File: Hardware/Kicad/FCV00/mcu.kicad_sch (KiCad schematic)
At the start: 35 parts, among them J1 USB_C_GCT_USB4105-GF-A, SW1 BOOT, U5 STM32F405RGT6, Y1 8MHz 12pF

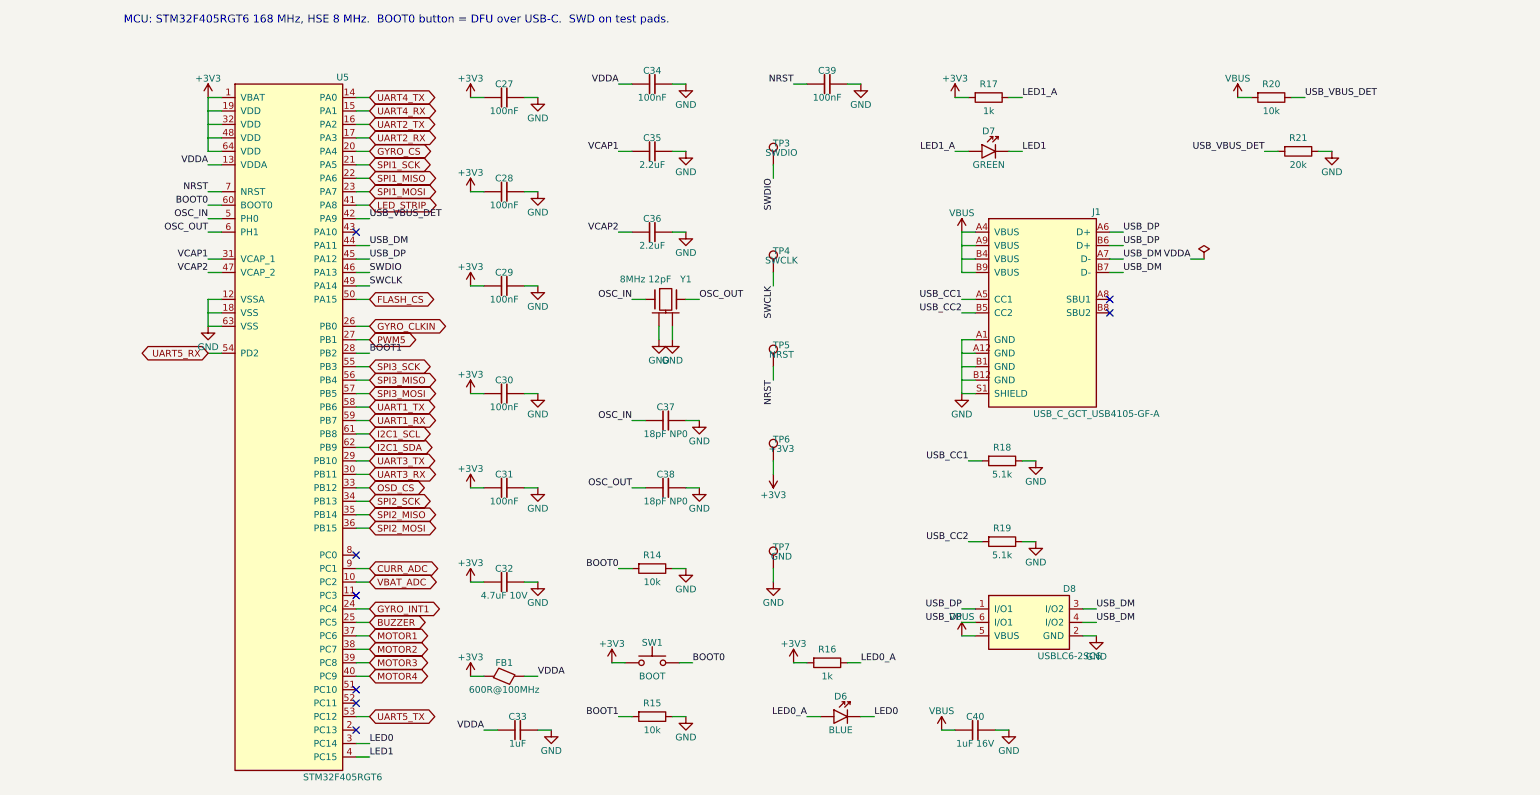
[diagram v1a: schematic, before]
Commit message: Boards follow the B0_EE part convention
- every real part uses the symbol/footprint/3D/datasheet named after its MPN in Kicad_Libs
- symbols keep only Reference, Value, Footprint, Datasheet, Description
  (MPN, Manufacturer, Verify, LCSC, Note fields removed; Verify notes moved to the Readme)
- schematic symbol caches rebuilt from the libraries, PCB footprints relinked with the
  same fields and 3D models as the library (connectivity unchanged)
- DNP and BOM attributes of the footprints match the symbols
- BOMs re-exported with kicad-cli
- ignore KiCad local history
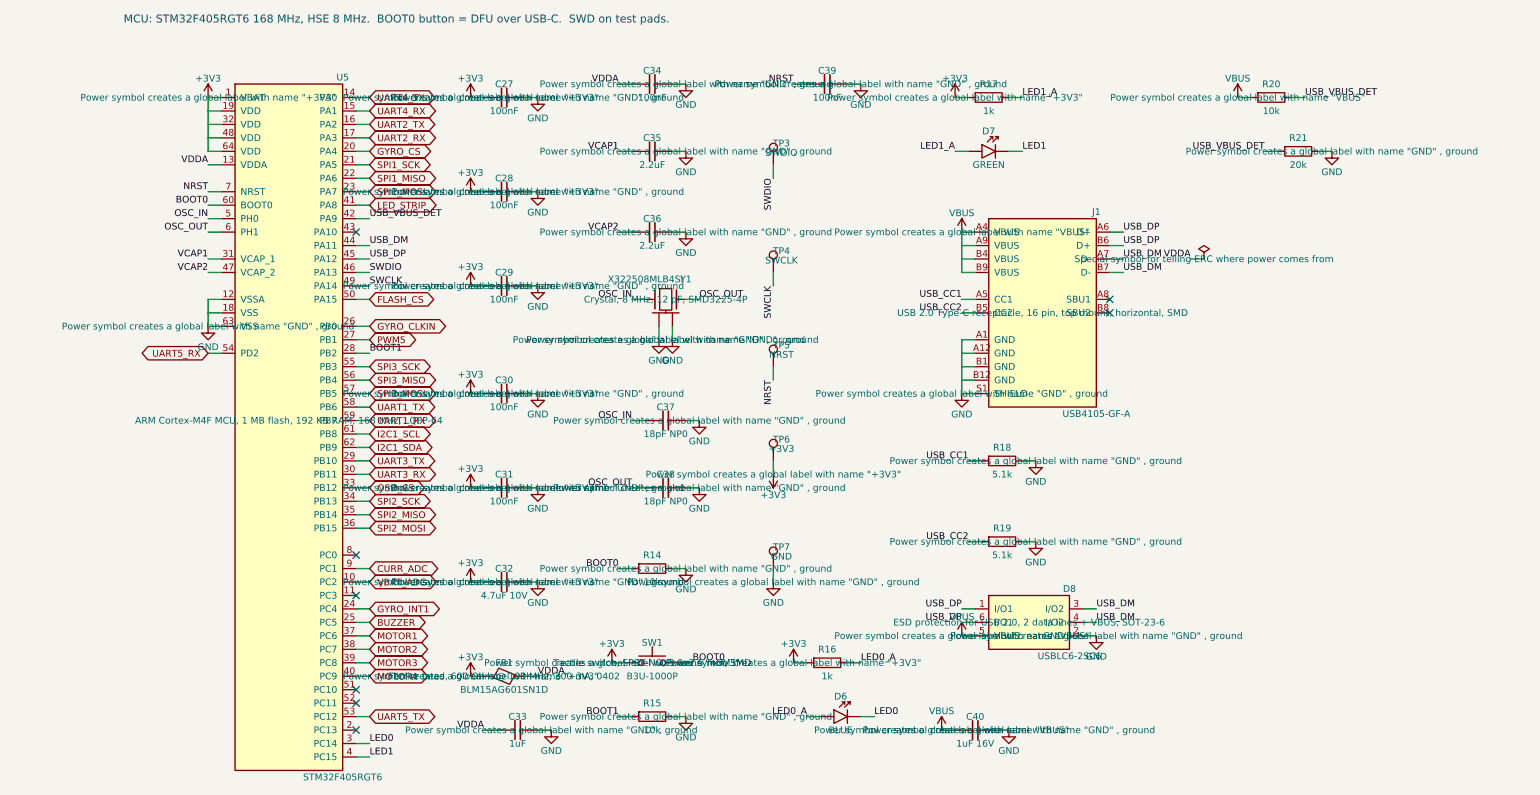
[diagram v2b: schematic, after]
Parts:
- D8: footprint eDiodes:SOT-23-6 -> eDiodes:USBLC6-2SC6; LCSC C7519 -> (none); MPN USBLC6-2SC6 -> (none); Manufacturer STMicroelectronics -> (none)
- FB1: value 600R@100MHz -> BLM15AG601SN1D; footprint eChoke:L_0402_1005Metric -> eFerrite:BLM15AG601SN1D; symbol eChoke:FB -> eFerrite:BLM15AG601SN1D; MPN BLM15AG601SN1D -> (none)
- J1: value USB_C_GCT_USB4105-GF-A -> USB4105-GF-A; footprint eConnector:USB_C_Receptacle_GCT_USB4105-xx-A_16P_TopMnt_Horizontal -> eConnector:USB4105-GF-A; symbol eConnector:USB_C_GCT_USB4105-GF-A -> eConnector:USB4105-GF-A; MPN USB4105-GF-A -> (none); Manufacturer GCT -> (none)
- SW1: value BOOT -> B3U-1000P; footprint eSwitch:SW_SPST_B3U-1000P -> eSwitch:B3U-1000P; symbol eSwitch:SW_Push -> eSwitch:B3U-1000P; MPN B3U-1000P -> (none); Manufacturer Omron -> (none)
- TP3, TP4, TP5, TP6, TP7: now left out of the parts list
- U5: footprint eMCU:LQFP-64_10x10mm_P0.5mm -> eMCU:STM32F405RGT6; LCSC C15742 -> (none); MPN STM32F405RGT6 -> (none); Manufacturer STMicroelectronics -> (none)
- Y1: value 8MHz 12pF -> X322508MLB4SI; footprint eCrystal:Crystal_SMD_3225-4Pin_3.2x2.5mm -> eCrystal:X322508MLB4SI; symbol eCrystal:Crystal_GND24 -> eCrystal:X322508MLB4SI; MPN X322508MLB4SI -> (none); Manufacturer Yangxing -> (none)

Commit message: Cleared all the descriptions and started Power section for FCV
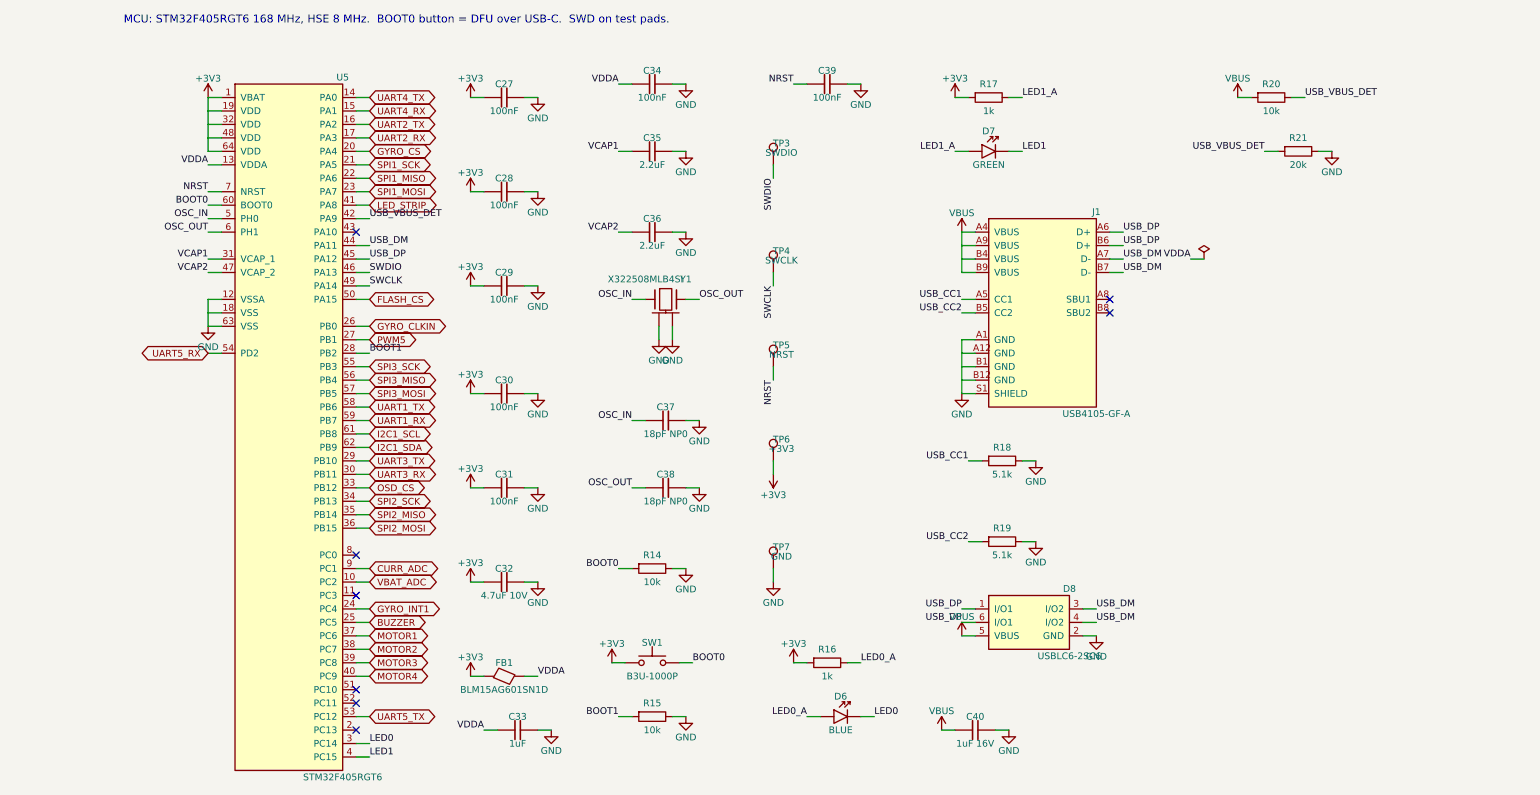
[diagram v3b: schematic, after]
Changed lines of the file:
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@@
 		(property "Description" "Power symbol creates a global label with name \"+3V3\""
 			(at 77.47 139.7 0)
+			(hide yes)
 			(show_name no)
 			(do_not_autoplace no)
@@
 		(property "Description" "Power symbol creates a global label with name \"GND\" , ground"
 			(at 120.65 91.44 0)
+			(hide yes)
 			(show_name no)
 			(do_not_autoplace no)
@@
 		(property "Description" "Crystal, 8 MHz, 12 pF, SMD3225-4P"
 			(at 114.3 68.58 0)
+			(hide yes)
 			(show_name no)
 			(do_not_autoplace no)
@@
 		(property "Description" "Power symbol creates a global label with name \"GND\" , ground"
 			(at 118.11 40.64 0)
+			(hide yes)
 			(show_name no)
 			(do_not_autoplace no)
@@
 		(property "Description" "Power symbol creates a global label with name \"+3V3\""
 			(at 77.47 86.36 0)
+			(hide yes)
 			(show_name no)
 			(do_not_autoplace no)
@@
 		(property "Description" "Power symbol creates a global label with name \"VBUS\""
 			(at 222.25 30.48 0)
+			(hide yes)
 			(show_name no)
 			(do_not_autoplace no)
@@
 		(property "Description" "Power symbol creates a global label with name \"GND\" , ground"
 			(at 90.17 48.26 0)
+			(hide yes)
 			(show_name no)
 			(do_not_autoplace no)
@@
 		(property "Description" "Power symbol creates a global label with name \"GND\" , ground"
 			(at 115.57 76.2 0)
+			(hide yes)
 			(show_name no)
 			(do_not_autoplace no)
@@
 		(property "Description" "Power symbol creates a global label with name \"GND\" , ground"
 			(at 92.71 149.86 0)
+			(hide yes)
 			(show_name no)
 			(do_not_autoplace no)
@@
 		(property "Description" "Power symbol creates a global label with name \"GND\" , ground"
 			(at 179.07 149.86 0)
+			(hide yes)
 			(show_name no)
 			(do_not_autoplace no)
@@
 		(property "Description" "Power symbol creates a global label with name \"GND\" , ground"
 			(at 90.17 121.92 0)
+			(hide yes)
 			(show_name no)
 			(do_not_autoplace no)
@@
 		(property "Description" "Special symbol for telling ERC where power comes from"
 			(at 215.9 60.96 0)
+			(hide yes)
 			(show_name no)
 			(do_not_autoplace no)
@@
 		(property "Description" "Power symbol creates a global label with name \"GND\" , ground"
 			(at 134.62 121.92 0)
+			(hide yes)
 			(show_name no)
 			(do_not_autoplace no)
@@
 		(property "Description" "Power symbol creates a global label with name \"+3V3\""
 			(at 134.62 101.6 0)
+			(hide yes)
 			(show_name no)
 			(do_not_autoplace no)
@@
 		(property "Description" "Power symbol creates a global label with name \"GND\" , ground"
 			(at 90.17 104.14 0)
+			(hide yes)
 			(show_name no)
 			(do_not_autoplace no)
@@
 		(property "Description" "Power symbol creates a global label with name \"GND\" , ground"
 			(at 151.13 27.94 0)
+			(hide yes)
 			(show_name no)
 			(do_not_autoplace no)
@@
 		(property "Description" "Power symbol creates a global label with name \"GND\" , ground"
 			(at 113.03 76.2 0)
+			(hide yes)
 			(show_name no)
 			(do_not_autoplace no)
@@
 		(property "Description" "Power symbol creates a global label with name \"GND\" , ground"
 			(at 118.11 119.38 0)
+			(hide yes)
 			(show_name no)
 			(do_not_autoplace no)
@@
 		(property "Description" "Power symbol creates a global label with name \"+3V3\""
 			(at 104.14 137.16 0)
+			(hide yes)
 			(show_name no)
 			(do_not_autoplace no)
@@
 		(property "Description" "Power symbol creates a global label with name \"GND\" , ground"
 			(at 170.18 86.36 0)
+			(hide yes)
 			(show_name no)
 			(do_not_autoplace no)
@@
 		(property "Description" "Power symbol creates a global label with name \"GND\" , ground"
 			(at 90.17 86.36 0)
+			(hide yes)
 			(show_name no)
 			(do_not_autoplace no)
@@
 		(property "Description" "Ferrite bead, 600 Ohm @ 100 MHz, 300 mA, 0402"
 			(at 83.82 139.7 0)
+			(hide yes)
 			(show_name no)
 			(do_not_autoplace no)
@@
 		(property "Description" "Power symbol creates a global label with name \"+3V3\""
 			(at 77.47 121.92 0)
+			(hide yes)
 			(show_name no)
 			(do_not_autoplace no)
@@
 		(property "Description" "USB 2.0 Type-C receptacle, 16 pin, top mount, horizontal, SMD"
 			(at 185.42 71.12 0)
+			(hide yes)
 			(show_name no)
 			(do_not_autoplace no)
@@
 		(property "Description" "Power symbol creates a global label with name \"+3V3\""
 			(at 138.43 137.16 0)
+			(hide yes)
 			(show_name no)
 			(do_not_autoplace no)
@@
 		(property "Description" "Power symbol creates a global label with name \"GND\" , ground"
 			(at 240.03 40.64 0)
+			(hide yes)
 			(show_name no)
 			(do_not_autoplace no)
@@
 		(property "Description" "Power symbol creates a global label with name \"VBUS\""
 			(at 166.37 149.86 0)
+			(hide yes)
 			(show_name no)
 			(do_not_autoplace no)
@@
 		(property "Description" "Power symbol creates a global label with name \"GND\" , ground"
 			(at 118.11 147.32 0)
+			(hide yes)
 			(show_name no)
 			(do_not_autoplace no)
@@
 		(property "Description" "Power symbol creates a global label with name \"GND\" , ground"
 			(at 184.15 114.3 0)
+			(hide yes)
 			(show_name no)
 			(do_not_autoplace no)
@@
 		(property "Description" "Power symbol creates a global label with name \"VBUS\""
 			(at 170.18 55.88 0)
+			(hide yes)
 			(show_name no)
 			(do_not_autoplace no)
@@
 		(property "Description" "Power symbol creates a global label with name \"+3V3\""
 			(at 168.91 30.48 0)
+			(hide yes)
 			(show_name no)
 			(do_not_autoplace no)
@@
 		(property "Description" "Power symbol creates a global label with name \"+3V3\""
 			(at 27.94 30.48 0)
+			(hide yes)
 			(show_name no)
 			(do_not_autoplace no)
@@
 		(property "Description" "Power symbol creates a global label with name \"+3V3\""
 			(at 77.47 30.48 0)
+			(hide yes)
 			(show_name no)
 			(do_not_autoplace no)
@@
 		(property "Description" "Power symbol creates a global label with name \"VBUS\""
 			(at 170.18 132.08 0)
+			(hide yes)
 			(show_name no)
 			(do_not_autoplace no)
@@
 		(property "Description" "ESD protection for USB 2.0, 2 data lines + VBUS, SOT-23-6"
 			(at 182.88 129.54 0)
+			(hide yes)
 			(show_name no)
 			(do_not_autoplace no)
@@
 		(property "Description" "Power symbol creates a global label with name \"+3V3\""
 			(at 77.47 66.04 0)
+			(hide yes)
 			(show_name no)
 			(do_not_autoplace no)
@@
 		(property "Description" "Power symbol creates a global label with name \"GND\" , ground"
 			(at 120.65 104.14 0)
+			(hide yes)
 			(show_name no)
 			(do_not_autoplace no)
@@
 		(property "Description" "Power symbol creates a global label with name \"GND\" , ground"
 			(at 27.94 73.66 0)
+			(hide yes)
 			(show_name no)
 			(do_not_autoplace no)
@@
 		(property "Description" "Power symbol creates a global label with name \"GND\" , ground"
 			(at 118.11 55.88 0)
+			(hide yes)
 			(show_name no)
 			(do_not_autoplace no)
@@
 		(property "Description" "Power symbol creates a global label with name \"GND\" , ground"
 			(at 90.17 30.48 0)
+			(hide yes)
 			(show_name no)
 			(do_not_autoplace no)
@@
 		(property "Description" "Power symbol creates a global label with name \"GND\" , ground"
 			(at 118.11 27.94 0)
+			(hide yes)
 			(show_name no)
 			(do_not_autoplace no)
@@
 		(property "Description" "Power symbol creates a global label with name \"GND\" , ground"
 			(at 195.58 132.08 0)
+			(hide yes)
 			(show_name no)
 			(do_not_autoplace no)
@@
 		(property "Description" "ARM Cortex-M4F MCU, 1 MB flash, 192 KB RAM, 168 MHz, LQFP-64"
 			(at 43.18 91.44 0)
+			(hide yes)
 			(show_name no)
 			(do_not_autoplace no)
@@
 		(property "Description" "Tactile switch, SPST-NO, 3.0x2.5 mm, SMD"
 			(at 111.76 137.16 0)
+			(hide yes)
 			(show_name no)
 			(do_not_autoplace no)
@@
 		(property "Description" "Power symbol creates a global label with name \"+3V3\""
 			(at 77.47 104.14 0)
+			(hide yes)
 			(show_name no)
 			(do_not_autoplace no)
@@
 		(property "Description" "Power symbol creates a global label with name \"GND\" , ground"
 			(at 90.17 66.04 0)
+			(hide yes)
 			(show_name no)
 			(do_not_autoplace no)
@@
 		(property "Description" "Power symbol creates a global label with name \"GND\" , ground"
 			(at 184.15 99.06 0)
+			(hide yes)
 			(show_name no)
 			(do_not_autoplace no)
@@
 		(property "Description" "Power symbol creates a global label with name \"+3V3\""
 			(at 77.47 48.26 0)
+			(hide yes)
 			(show_name no)
 			(do_not_autoplace no)
